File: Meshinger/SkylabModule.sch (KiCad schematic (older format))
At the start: 4 parts, among them J2 Micro_SD_Card, Q2 NTR2101P, U4 BBQ10KBD, U5 SKW92A

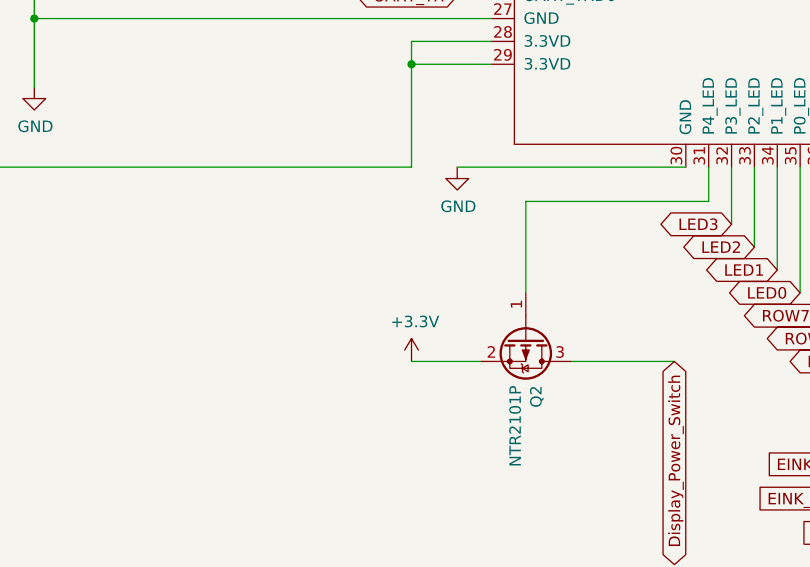
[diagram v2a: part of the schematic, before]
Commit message: Meshinger 1.0 rev D, now with power switch and squiggles.
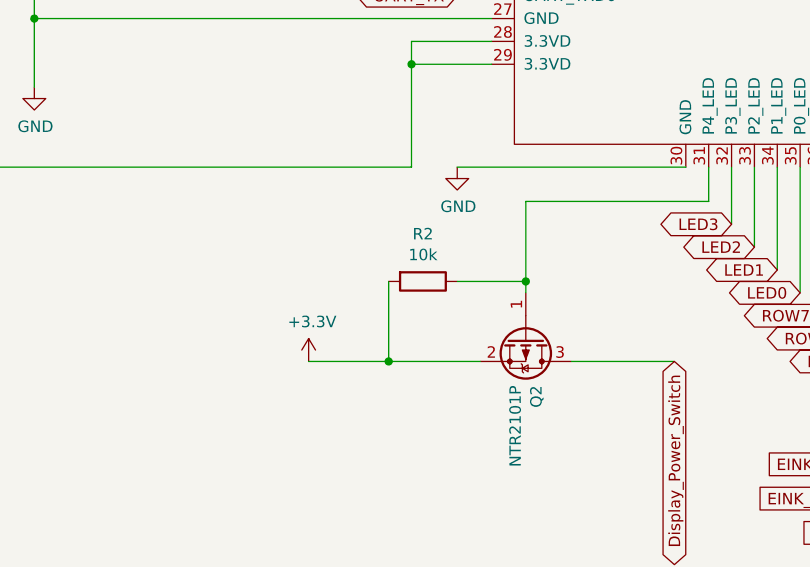
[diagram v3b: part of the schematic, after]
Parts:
- added R2: 10k, Resistor_SMD:R_0805_2012Metric_Pad1.20x1.40mm_HandSolder, symbol Device:R
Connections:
- net +3V3: now also R2.2
- net at Q2.1 (G), U5.31 (P4_LED): now also R2.1
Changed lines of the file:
@@
 L power:+3.3V #PWR013
 U 1 1 603F3686
-P 6600 5150
-F 0 "#PWR013" H 6600 5000 50  0001 C CNN
-F 1 "+3.3V" H 6615 5323 50  0000 C CNN
-F 2 "" H 6600 5150 50  0001 C CNN
-F 3 "" H 6600 5150 50  0001 C CNN
-	1    6600 5150
+P 6150 5150
+F 0 "#PWR013" H 6150 5000 50  0001 C CNN
+F 1 "+3.3V" H 6165 5323 50  0000 C CNN
+F 2 "" H 6150 5150 50  0001 C CNN
+F 3 "" H 6150 5150 50  0001 C CNN
+	1    6150 5150
 	1    0    0    -1
 $EndComp
-Wire Wire Line
-	6600 5150 6900 5150
 Text GLabel 7750 5150 3    50   BiDi ~ 0
 Display_Power_Switch
@@
 	7900 4450 7100 4450
 Wire Wire Line
-	7100 4450 7100 4850
+	7100 4450 7100 4800
+Wire Wire Line
+	6150 5150 6500 5150
+$Comp
+L Device:R R2
+U 1 1 617BE3EA
+P 6650 4800
+F 0 "R2" V 6443 4800 50  0000 C CNN
+F 1 "10k" V 6534 4800 50  0000 C CNN
+F 2 "Resistor_SMD:R_0805_2012Metric_Pad1.20x1.40mm_HandSolder" V 6535 4800 50  0001 C CNN
+F 3 "~" H 6650 4800 50  0001 C CNN
+	1    6650 4800
+	0    1    1    0
+$EndComp
+Wire Wire Line
+	6800 4800 7100 4800
+Connection ~ 7100 4800
+Wire Wire Line
+	7100 4800 7100 4850
+Wire Wire Line
+	6500 4800 6500 5150
+Connection ~ 6500 5150
+Wire Wire Line
+	6500 5150 6900 5150
 $EndSCHEMATC
